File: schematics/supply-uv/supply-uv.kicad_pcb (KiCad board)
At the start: 2 copper layers, 100 x 100 mm, 88 parts, among them J1 Conn_01x02_Pin, J2 Conn_01x01_Pin, J3 CW2B-10A-T, K1 SRD-12VDC-SL-C, Q1 IRLML5203, U1 ICE2PCS01, U2 TL331, U3 R7731, U4 EL817, U5 TL432DBZ, Y1 B32022A3223M000

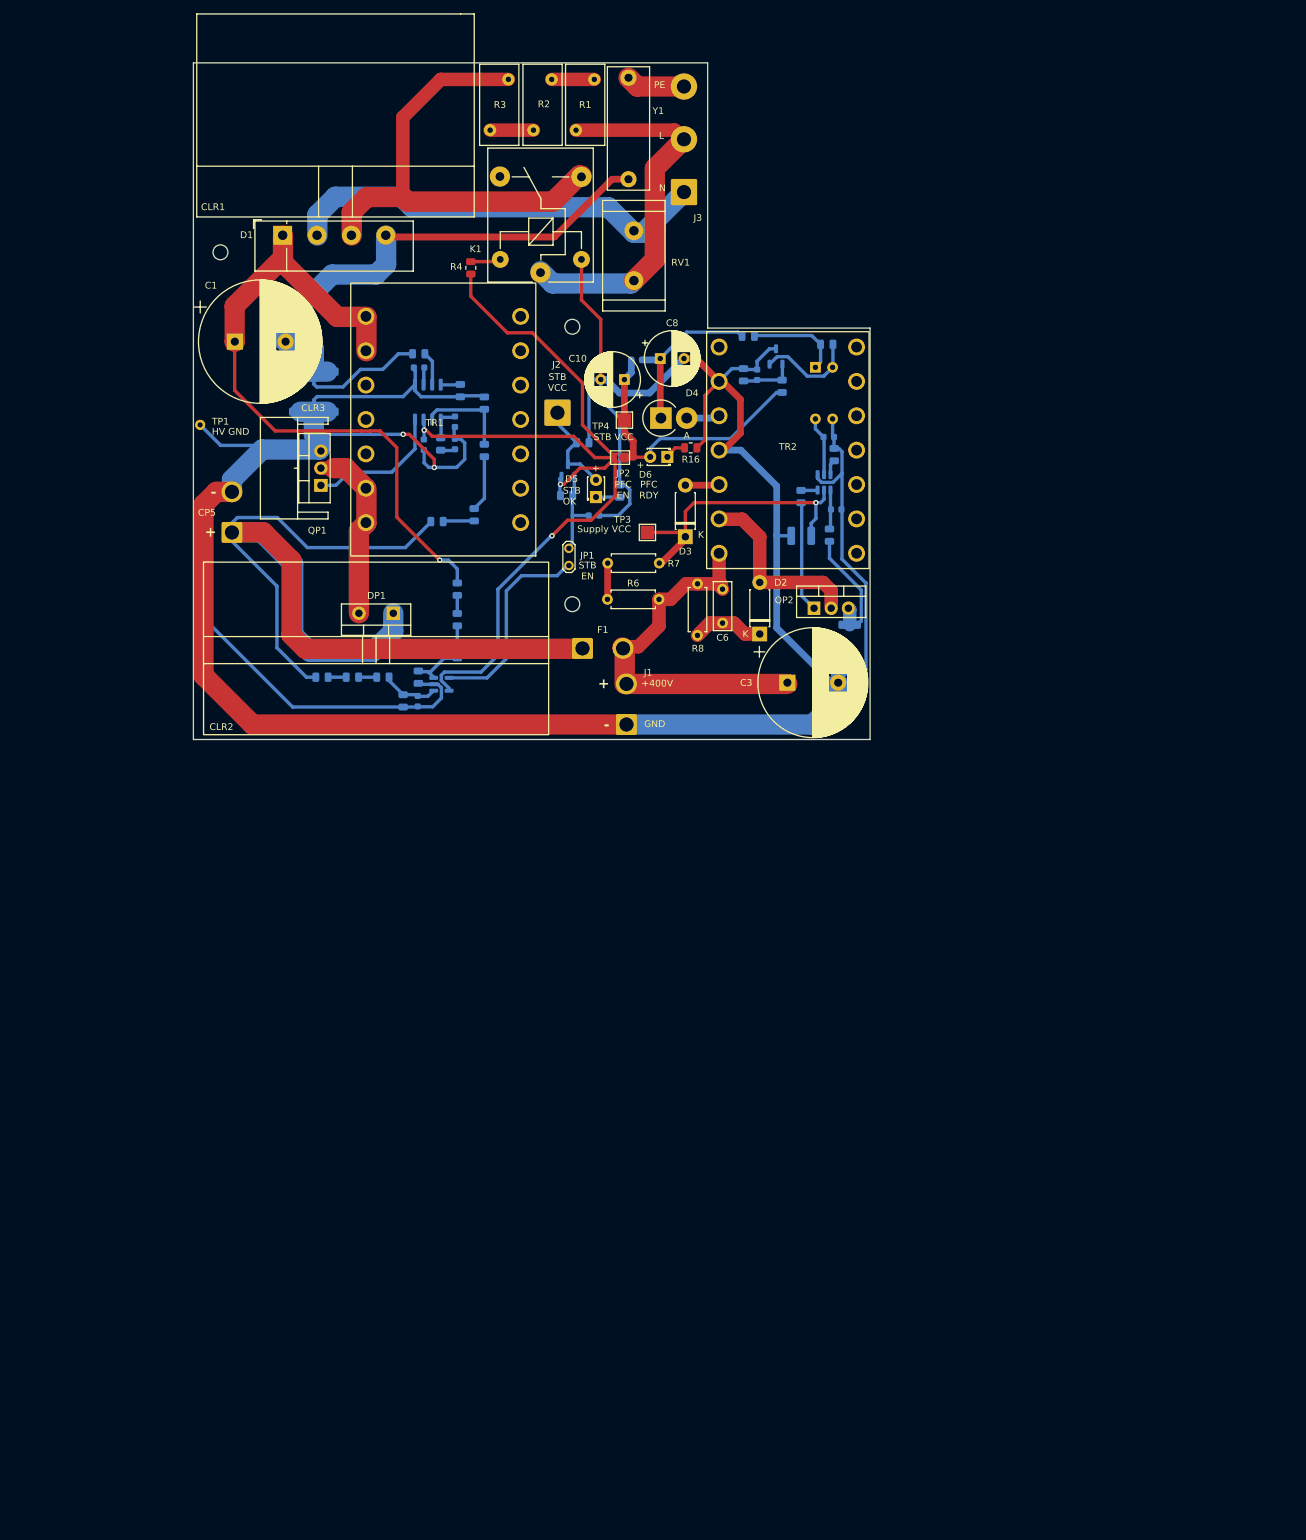
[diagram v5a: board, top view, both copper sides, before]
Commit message: Board#1 schematics rewrited
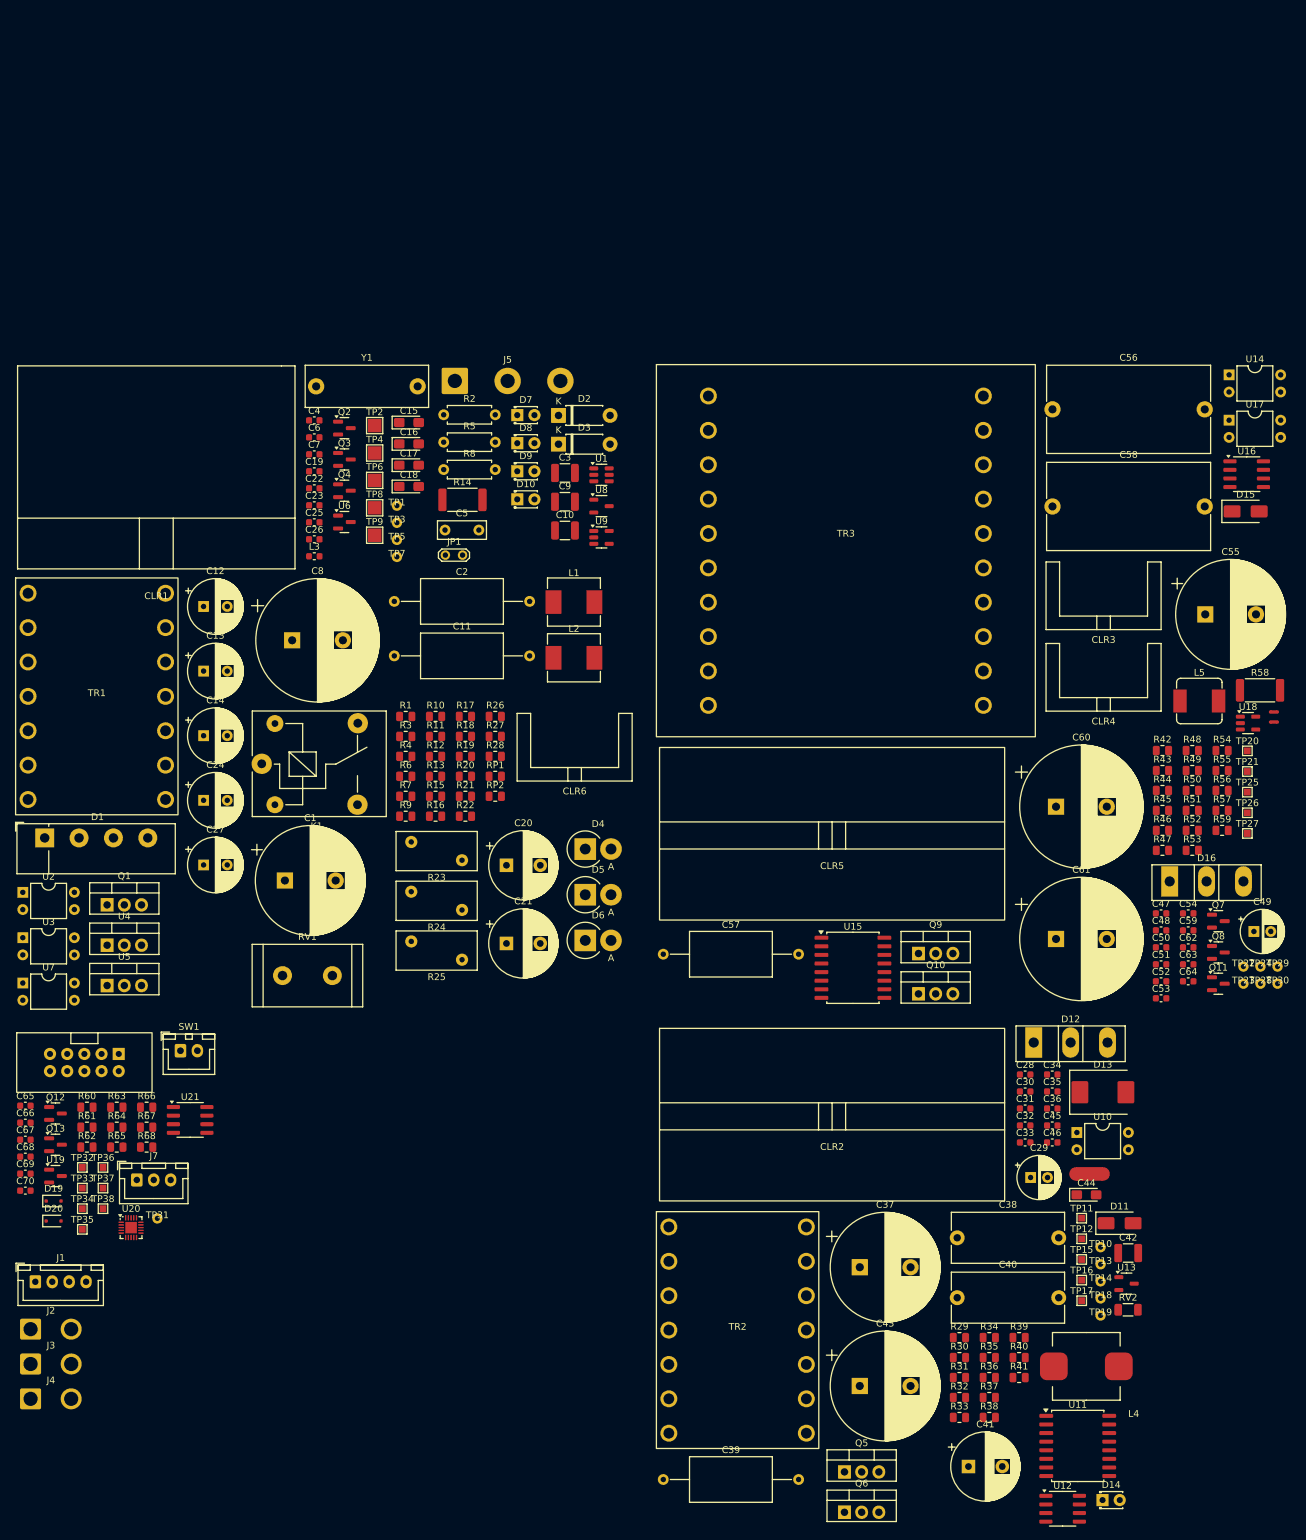
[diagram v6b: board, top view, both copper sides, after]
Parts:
- removed CP1, CP3: 100 nF, Capacitor_SMD:C_0603_1608Metric
- removed CP2, CP4: 1 uF, Capacitor_SMD:C_0603_1608Metric
- removed CP5: 3300 uF@450V, Connector_Wire:SolderWire-1.5sqmm_1x02_P6mm_D1.7mm_OD3mm
- removed DP1: STTH8S06D, Package_TO_SOT_THT:TO-220-2_Vertical
- removed F1: C10G4 with fuseholder, Connector_Wire:SolderWire-1.5sqmm_1x02_P6mm_D1.7mm_OD3mm
- removed H1, H2, H3: MountingHole, MountingHole:MountingHole_2.2mm_M2
- removed JP2: PFC Enable, Jumper:SolderJumper-2_P1.3mm_Open_TrianglePad1.0x1.5mm
- removed QP1, QP2: STP13NK60Z, Package_TO_SOT_THT:TO-220-3_Vertical
- removed RP10, RP9: 680K, Resistor_SMD:R_0805_2012Metric
- removed RP11: 620K, Resistor_SMD:R_0805_2012Metric
- removed RP12: 15K, Resistor_SMD:R_0805_2012Metric
- removed RP13, RP14, RP15, RP5, RP6, RP7: 750K, Resistor_SMD:R_0805_2012Metric
- removed RP16: 68K, Resistor_SMD:R_0805_2012Metric
- removed RP17: 0.12, Resistor_SMD:R_2512_6332Metric
- removed RP3: 10K, Resistor_SMD:R_0805_2012Metric
- removed RP4: 220, Resistor_SMD:R_0805_2012Metric
- removed RP8: 75K, Resistor_SMD:R_0805_2012Metric
- added C12: 220 uF@35V, Capacitor_THT:CP_Radial_D8.0mm_P3.50mm, F.Cu at (64.5, 124.3)
- added C13: 220 uF@35V, Capacitor_THT:CP_Radial_D8.0mm_P3.50mm, F.Cu at (64.5, 133.9)
- added C14: 220 uF@35V, Capacitor_THT:CP_Radial_D8.0mm_P3.50mm, F.Cu at (64.5, 143.4)
- added C15: 22 uF, Capacitor_Tantalum_SMD:CP_EIA-3216-10_Kemet-I_Pad1.58x1.35mm_HandSolder, F.Cu at (94.9, 97.2)
- added C16: 22 uF, Capacitor_Tantalum_SMD:CP_EIA-3216-10_Kemet-I_Pad1.58x1.35mm_HandSolder, F.Cu at (94.9, 100.3)
- added C17: 22 uF, Capacitor_Tantalum_SMD:CP_EIA-3216-10_Kemet-I_Pad1.58x1.35mm_HandSolder, F.Cu at (94.9, 103.5)
- added C18: 22 uF, Capacitor_Tantalum_SMD:CP_EIA-3216-10_Kemet-I_Pad1.58x1.35mm_HandSolder, F.Cu at (94.9, 106.6)
- added C19: 10 nF, Capacitor_SMD:C_0603_1608Metric, F.Cu at (80.9, 104.4)
- added C20: 1000 uF@16V, Capacitor_THT:CP_Radial_D10.0mm_P5.00mm, F.Cu at (109.3, 162.6)
- added C21: 1000 uF@16V, Capacitor_THT:CP_Radial_D10.0mm_P5.00mm, F.Cu at (109.3, 174.1)
- added C22: 4.7 uF, Capacitor_SMD:C_0603_1608Metric, F.Cu at (80.9, 106.9)
- added C23: 10 nF, Capacitor_SMD:C_0603_1608Metric, F.Cu at (80.9, 109.4)
- added C24: 220 uF@35V, Capacitor_THT:CP_Radial_D8.0mm_P3.50mm, F.Cu at (64.5, 153.0)
- added C25: 100 nF, Capacitor_SMD:C_0603_1608Metric, F.Cu at (80.9, 111.9)
- added C26: 1 uF, Capacitor_SMD:C_0603_1608Metric, F.Cu at (80.9, 114.4)
- added C27: 220 uF@35V, Capacitor_THT:CP_Radial_D8.0mm_P3.50mm, F.Cu at (64.5, 162.5)
- added C28: 100 nF, Capacitor_SMD:C_0603_1608Metric, F.Cu at (185.9, 193.5)
- added C29: 47 uF@35V, Capacitor_THT:CP_Radial_D6.3mm_P2.50mm, F.Cu at (186.7, 208.7)
- added C30: 10 uF, Capacitor_SMD:C_0603_1608Metric, F.Cu at (185.9, 196.0)
- added C31: 100 nF, Capacitor_SMD:C_0603_1608Metric, F.Cu at (185.9, 198.5)
- added C32: 2.2 nF, Capacitor_SMD:C_0603_1608Metric, F.Cu at (185.9, 201.0)
- added C33: 10 uF, Capacitor_SMD:C_0603_1608Metric, F.Cu at (185.9, 203.6)
- added C34: 100 nF, Capacitor_SMD:C_0603_1608Metric, F.Cu at (189.9, 193.5)
- added C35: 100 nF, Capacitor_SMD:C_0603_1608Metric, F.Cu at (189.9, 196.0)
- added C36: 1 uF, Capacitor_SMD:C_0603_1608Metric, F.Cu at (189.9, 198.5)
- added C37: 47 uF@450V, Capacitor_THT:CP_Radial_D16.0mm_P7.50mm, F.Cu at (161.5, 222.0)
- added C38: К73-17 0.15 uF@400V, Capacitor_THT:C_Rect_L16.5mm_W7.3mm_P15.00mm_MKT, F.Cu at (175.9, 217.6)
- added C39: К73-17 0.22 uF@630V, Capacitor_THT:C_Axial_L12.0mm_D6.5mm_P20.00mm_Horizontal, F.Cu at (132.4, 253.4)
- added C40: К73-17 0.15 uF@400V, Capacitor_THT:C_Rect_L16.5mm_W7.3mm_P15.00mm_MKT, F.Cu at (175.9, 226.5)
- added C41: 1000 uF@16V, Capacitor_THT:CP_Radial_D10.0mm_P5.00mm, F.Cu at (177.5, 251.4)
- added C42: 22 uF, Capacitor_SMD:C_1210_3225Metric, F.Cu at (201.2, 219.9)
- added C43: 2200 uF@35V, Capacitor_THT:CP_Radial_D16.0mm_P7.50mm, F.Cu at (161.5, 239.5)
- added C44: 22 uF, Capacitor_Tantalum_SMD:CP_EIA-3216-10_Kemet-I_Pad1.58x1.35mm_HandSolder, F.Cu at (195.0, 211.3)
- added C45: 100 nF, Capacitor_SMD:C_0603_1608Metric, F.Cu at (189.9, 201.0)
- added C46: 1 uF, Capacitor_SMD:C_0603_1608Metric, F.Cu at (189.9, 203.6)
- added C47: 100 nF, Capacitor_SMD:C_0603_1608Metric, F.Cu at (206.0, 169.7)
- added C48: 10 uF, Capacitor_SMD:C_0603_1608Metric, F.Cu at (206.0, 172.2)
- added C49: 47 uF@35V, Capacitor_THT:CP_Radial_D6.3mm_P2.50mm, F.Cu at (219.7, 172.4)
- added C50: 10 uF, Capacitor_SMD:C_0603_1608Metric, F.Cu at (206.0, 174.7)
- added C51: 2.2 nF, Capacitor_SMD:C_0603_1608Metric, F.Cu at (206.0, 177.2)
- added C52: 100 nF, Capacitor_SMD:C_0603_1608Metric, F.Cu at (206.0, 179.7)
- added C53: 100 nF, Capacitor_SMD:C_0603_1608Metric, F.Cu at (206.0, 182.2)
- added C54: 1 uF, Capacitor_SMD:C_0603_1608Metric, F.Cu at (210.0, 169.7)
- added C55: 47 uF@450V, Capacitor_THT:CP_Radial_D16.0mm_P7.50mm, F.Cu at (212.5, 125.5)
- added C56: К73-17 1 uF@400V, Capacitor_THT:C_Rect_L24.0mm_W12.8mm_P22.50mm_MKT, F.Cu at (190.0, 95.2)
- added C57: К73-17 0.22 uF@630V, Capacitor_THT:C_Axial_L12.0mm_D6.5mm_P20.00mm_Horizontal, F.Cu at (132.4, 175.7)
- added C58: К73-17 1 uF@400V, Capacitor_THT:C_Rect_L24.0mm_W12.8mm_P22.50mm_MKT, F.Cu at (190.0, 109.6)
- added C59: 100 nF, Capacitor_SMD:C_0603_1608Metric, F.Cu at (210.0, 172.2)
- added C60: 2200 uF@63V, Capacitor_THT:CP_Radial_D18.0mm_P7.50mm, F.Cu at (190.5, 153.9)
- added C61: 2200 uF@63V, Capacitor_THT:CP_Radial_D18.0mm_P7.50mm, F.Cu at (190.5, 173.5)
- added C62: 10 nF, Capacitor_SMD:C_0603_1608Metric, F.Cu at (210.0, 174.7)
- added C63: 10 nF, Capacitor_SMD:C_0603_1608Metric, F.Cu at (210.0, 177.2)
- added C64: 1 uF, Capacitor_SMD:C_0603_1608Metric, F.Cu at (210.0, 179.7)
- added C65: 100 nF, Capacitor_SMD:C_0603_1608Metric, F.Cu at (38.2, 198.1)
- added C66: 4.7 uF, Capacitor_SMD:C_0603_1608Metric, F.Cu at (38.2, 200.6)
- added C67: 220 nF, Capacitor_SMD:C_0603_1608Metric, F.Cu at (38.2, 203.1)
- added C68: 100 nF, Capacitor_SMD:C_0603_1608Metric, F.Cu at (38.2, 205.7)
- added C69: 100 nF, Capacitor_SMD:C_0603_1608Metric, F.Cu at (38.2, 208.2)
- added C70: 1 uF, Capacitor_SMD:C_0603_1608Metric, F.Cu at (38.2, 210.7)
- added CLR4: HS 239-20, Library:HS-239-20, F.Cu at (197.5, 139.8)
- added CLR5: HS 216-30@30х51х25.5mm, Library:HS 216-30, F.Cu at (157.4, 158.2)
- added CLR6: HS 239-20, Library:HS-239-20, F.Cu at (119.3, 150.1)
- added D10: L-2060YD, LED_THT:LED_D1.8mm_W3.3mm_H2.4mm, F.Cu at (110.9, 108.5)
- added D11: STTH1R06A, Diode_SMD:D_SMA, F.Cu at (199.9, 215.5)
- added D12: STTH3003CW, Package_TO_SOT_THT:TO-247-3_Vertical, F.Cu at (187.2, 188.8)
- added D13: SMCJ5.0A, Diode_SMD:D_SMC, F.Cu at (197.4, 196.1)
- added D14: L-2060YD, LED_THT:LED_D1.8mm_W3.3mm_H2.4mm, F.Cu at (197.4, 256.4)
- added D15: STTH1R06A, Diode_SMD:D_SMA, F.Cu at (218.5, 110.3)
- added D16: STTH3003CW, Package_TO_SOT_THT:TO-247-3_Vertical, F.Cu at (207.3, 165.0)
- added D19: BAV21WS, Diode_SMD:D_SOD-323F, F.Cu at (42.3, 212.2)
- added D20: BAV21WS, Diode_SMD:D_SOD-323F, F.Cu at (42.3, 215.2)
- added D7: L-2060YD, LED_THT:LED_D1.8mm_W3.3mm_H2.4mm, F.Cu at (110.9, 96.1)
- added D8: L-2060YD, LED_THT:LED_D1.8mm_W3.3mm_H2.4mm, F.Cu at (110.9, 100.2)
- added D9: L-2060YD, LED_THT:LED_D1.8mm_W3.3mm_H2.4mm, F.Cu at (110.9, 104.4)
- added J4: PWR_OUT (with fuse), Connector_Wire:SolderWire-1.5sqmm_1x02_P6mm_D1.7mm_OD3mm, F.Cu at (38.9, 241.4)
- added J5: CW2B-10A-T, Connector_Wire:SolderWire-1.5sqmm_1x03_P7.8mm_D1.7mm_OD3.9mm, F.Cu at (101.6, 91.0)
- added J6: USBASP, Library:DC3-2x05_p2.54, F.Cu at (46.9, 191.7)
- added J7: JST XH B3B, Connector_JST:JST_XH_B3B-XH-A_1x03_P2.50mm_Vertical, F.Cu at (54.6, 209.1)
- added L2: 22 uH@0650, Inductor_SMD:L_Chilisin_BMRB00060650, F.Cu at (119.2, 131.9)
- added L3: BLM18EG221SN1D, Inductor_SMD:L_0603_1608Metric, F.Cu at (80.9, 116.9)
- added L4: HPI1040-1R0, Library:Ferrocore-HPI1040, F.Cu at (195.0, 236.6)
- added L5: SPM6550T-R68M, Inductor_SMD:L_Sumida_CDMC6D28_7.25x6.5mm, F.Cu at (211.7, 138.3)
- added NT1: STB2HV_GND, NetTie:NetTie-2_SMD_Pad2.0mm, F.Cu at (195.4, 208.2)
- added NT2: STB2HV_GND, NetTie:NetTie-2_SMD_Pad0.5mm, F.Cu at (222.7, 139.9)
- added NT3: VSYS_PWR2PWR_OUT_GND, NetTie:NetTie-2_SMD_Pad0.5mm, F.Cu at (222.7, 141.4)
- added Q10: STP13NK60Z, Package_TO_SOT_THT:TO-220-3_Vertical, F.Cu at (170.2, 181.6)
- added Q11: IRLML0030, Package_TO_SOT_SMD:SOT-23, F.Cu at (214.5, 180.1)
- added Q12: IRLML0030, Package_TO_SOT_SMD:SOT-23, F.Cu at (42.6, 199.3)
- added Q13: IRLML0030, Package_TO_SOT_SMD:SOT-23, F.Cu at (42.6, 203.9)
- added Q2: IRLML5203, Package_TO_SOT_SMD:SOT-23, F.Cu at (85.3, 98.0)
- added Q3: IRLML5203, Package_TO_SOT_SMD:SOT-23, F.Cu at (85.3, 102.6)
- added Q4: IRLML5203, Package_TO_SOT_SMD:SOT-23, F.Cu at (85.3, 107.2)
- added Q5: STP13NK60Z, Package_TO_SOT_THT:TO-220-3_Vertical, F.Cu at (159.2, 252.2)
- added Q6: STP13NK60Z, Package_TO_SOT_THT:TO-220-3_Vertical, F.Cu at (159.2, 258.2)
- added Q7: IRLML0030, Package_TO_SOT_SMD:SOT-23, F.Cu at (214.5, 170.8)
- added Q8: IRLML0030, Package_TO_SOT_SMD:SOT-23, F.Cu at (214.5, 175.5)
- added Q9: STP13NK60Z, Package_TO_SOT_THT:TO-220-3_Vertical, F.Cu at (170.2, 175.6)
- added R20: 39K, Resistor_SMD:R_0805_2012Metric, F.Cu at (103.2, 149.4)
- added R21: 3K, Resistor_SMD:R_0805_2012Metric, F.Cu at (103.2, 152.4)
- added R22: 1K, Resistor_SMD:R_0805_2012Metric, F.Cu at (103.2, 155.3)
- added R23: JNR13S500L, Varistor:RV_Disc_D12mm_W5.8mm_P7.5mm, F.Cu at (95.2, 159.1)
- added R24: JNR13S500L, Varistor:RV_Disc_D12mm_W5.8mm_P7.5mm, F.Cu at (95.2, 166.5)
- added R25: JNR13S500L, Varistor:RV_Disc_D12mm_W5.8mm_P7.5mm, F.Cu at (95.2, 173.8)
- added R26: 150, Resistor_SMD:R_0805_2012Metric, F.Cu at (107.6, 140.6)
- added R27: 10K, Resistor_SMD:R_0805_2012Metric, F.Cu at (107.6, 143.5)
- added R28: 1K, Resistor_SMD:R_0805_2012Metric, F.Cu at (107.6, 146.5)
- added R29: 680, Resistor_SMD:R_0805_2012Metric, F.Cu at (176.2, 232.4)
- added R30: 2K, Resistor_SMD:R_0805_2012Metric, F.Cu at (176.2, 235.3)
- added R31: 10K, Resistor_SMD:R_0805_2012Metric, F.Cu at (176.2, 238.3)
- added R32: 10K, Resistor_SMD:R_0805_2012Metric, F.Cu at (176.2, 241.2)
- added R33: 4K7, Resistor_SMD:R_0805_2012Metric, F.Cu at (176.2, 244.2)
- added R34: 2K2, Resistor_SMD:R_0805_2012Metric, F.Cu at (180.6, 232.4)
- added R35: 22, Resistor_SMD:R_0805_2012Metric, F.Cu at (180.6, 235.3)
- added R36: 10, Resistor_SMD:R_0805_2012Metric, F.Cu at (180.6, 238.3)
- added R37: 10, Resistor_SMD:R_0805_2012Metric, F.Cu at (180.6, 241.2)
- added R38: 150, Resistor_SMD:R_0805_2012Metric, F.Cu at (180.6, 244.2)
- added R39: 10K, Resistor_SMD:R_0805_2012Metric, F.Cu at (185.0, 232.4)
- added R40: 3K3, Resistor_SMD:R_0805_2012Metric, F.Cu at (185.0, 235.3)
- added R41: 510, Resistor_SMD:R_0805_2012Metric, F.Cu at (185.0, 238.3)
- added R42: 10K, Resistor_SMD:R_0805_2012Metric, F.Cu at (206.2, 145.6)
- added R43: 10K, Resistor_SMD:R_0805_2012Metric, F.Cu at (206.2, 148.6)
- added R44: 2K, Resistor_SMD:R_0805_2012Metric, F.Cu at (206.2, 151.5)
- added R45: 2K2, Resistor_SMD:R_0805_2012Metric, F.Cu at (206.2, 154.5)
- added R46: 10K, Resistor_SMD:R_0805_2012Metric, F.Cu at (206.2, 157.4)
- added R47: 22, Resistor_SMD:R_0805_2012Metric, F.Cu at (206.2, 160.4)
- added R48: 2K, Resistor_SMD:R_0805_2012Metric, F.Cu at (210.6, 145.6)
- added R49: 10K, Resistor_SMD:R_0805_2012Metric, F.Cu at (210.6, 148.6)
- added R50: 10K, Resistor_SMD:R_0805_2012Metric, F.Cu at (210.6, 151.5)
- added R51: 10, Resistor_SMD:R_0805_2012Metric, F.Cu at (210.6, 154.5)
- added R52: 10, Resistor_SMD:R_0805_2012Metric, F.Cu at (210.6, 157.4)
- added R53: 2K, Resistor_SMD:R_0805_2012Metric, F.Cu at (210.6, 160.4)
- added R54: 2K, Resistor_SMD:R_0805_2012Metric, F.Cu at (215.0, 145.6)
- added R55: 10K, Resistor_SMD:R_0805_2012Metric, F.Cu at (215.0, 148.6)
- added R56: 9K1, Resistor_SMD:R_0805_2012Metric, F.Cu at (215.0, 151.5)
- added R57: 1K, Resistor_SMD:R_0805_2012Metric, F.Cu at (215.0, 154.5)
- added R58: 0.01, Resistor_SMD:R_2512_6332Metric, F.Cu at (220.6, 136.7)
- added R59: 47K, Resistor_SMD:R_0805_2012Metric, F.Cu at (215.0, 157.4)
- added R60: 510, Resistor_SMD:R_0805_2012Metric, F.Cu at (47.3, 198.3)
- added R61: 10K, Resistor_SMD:R_0805_2012Metric, F.Cu at (47.3, 201.3)
- added R62: 10K, Resistor_SMD:R_0805_2012Metric, F.Cu at (47.3, 204.2)
- added R63: 220, Resistor_SMD:R_0805_2012Metric, F.Cu at (51.7, 198.3)
- added R64: 10K, Resistor_SMD:R_0805_2012Metric, F.Cu at (51.7, 201.3)
- added R65: 220, Resistor_SMD:R_0805_2012Metric, F.Cu at (51.7, 204.2)
- added R66: 10K, Resistor_SMD:R_0805_2012Metric, F.Cu at (56.1, 198.3)
- added R67: 10K, Resistor_SMD:R_0805_2012Metric, F.Cu at (56.1, 201.3)
- added R68: 10K, Resistor_SMD:R_0805_2012Metric, F.Cu at (56.1, 204.2)
- added RV2: CT1206M6G, Resistor_SMD:R_1206_3216Metric, F.Cu at (201.1, 228.3)
- added SW1: SW_Push, Connector_JST:JST_XH_B2B-XH-A_1x02_P2.50mm_Vertical, F.Cu at (61.1, 190.0)
- added TP10: +5V_FEEDBACK, Library:TestPoint_Plated_Hole_D1.0mm, F.Cu at (197.1, 219.0)
- added TP11: 5V_H, TestPoint:TestPoint_Pad_1.0x1.0mm, F.Cu at (194.3, 214.7)
- added TP12: 5V_L, TestPoint:TestPoint_Pad_1.0x1.0mm, F.Cu at (194.3, 217.8)
- added TP13: STB_GND, Library:TestPoint_Plated_Hole_D1.0mm, F.Cu at (197.1, 221.6)
- added TP14: HV_GND, Library:TestPoint_Plated_Hole_D1.0mm, F.Cu at (197.1, 224.1)
- added TP15: 5V_GH, TestPoint:TestPoint_Pad_1.0x1.0mm, F.Cu at (194.3, 220.8)
- added TP16: 5V_GL, TestPoint:TestPoint_Pad_1.0x1.0mm, F.Cu at (194.3, 223.9)
- added TP17: 5V_MP, TestPoint:TestPoint_Pad_1.0x1.0mm, F.Cu at (194.3, 226.9)
- added TP18: +5V_PWR, Library:TestPoint_Plated_Hole_D1.0mm, F.Cu at (197.1, 226.6)
- added TP19: +5V_GND, Library:TestPoint_Plated_Hole_D1.0mm, F.Cu at (197.1, 229.1)
- added TP2: Supply VCC, TestPoint:TestPoint_Pad_2.0x2.0mm, F.Cu at (89.8, 97.6)
- added TP20: PV_H, TestPoint:TestPoint_Pad_1.0x1.0mm, F.Cu at (218.8, 145.7)
- added TP21: PV_L, TestPoint:TestPoint_Pad_1.0x1.0mm, F.Cu at (218.8, 148.7)
- added TP22: PWR_SHUTDOWN, Library:TestPoint_Plated_Hole_D1.0mm, F.Cu at (218.2, 177.6)
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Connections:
- net Net-(D5-K) renamed /standby Sheet/VSYS1_PRE_VCC
- C1 pad 1: /Input power with filter/VOUT_PRE_PFC -> /5V_PWR Sheet/HV_VCC
- C1 pad 2: /Input power with filter/VOUT_PRE_GND -> /5V_PWR Sheet/HV_GND
- C10 pad 1: Net-(D6-A) -> /pwrcontrol Sheet/VSYS_PWR_GND
- C10 pad 2: /Input power with filter/HV_GND -> Net-(Q3-D)
- C11 pad 1: /Input power with filter/HV_GND -> /5V_PWR Sheet/HV_GND
- C11 pad 2: Net-(JP1-B) -> /5V_PWR Sheet/HV_VCC
- C2 pad 1: Net-(U2--) -> /5V_PWR Sheet/HV_GND
- C2 pad 2: /Input power with filter/HV_GND -> /5V_PWR Sheet/HV_VCC
- C3 pad 1: /Input power with filter/OUT_400V -> /5V_PWR Sheet/HV_GND
- C3 pad 2: /Input power with filter/HV_GND -> Net-(D2-K)
- C4 pad 1: /Input power with filter/HV_GND -> /5V_PWR Sheet/HV_GND
- C4 pad 2: Net-(D3-K) -> Net-(U1-CS)
- C5 pad 1: /Input power with filter/HV_GND -> Net-(D3-K)
- C5 pad 2: Net-(U3-CS) -> /5V_PWR Sheet/HV_VCC
- C6 pad 1: Net-(D2-K) -> /VSYS_GND
- C6 pad 2: /Input power with filter/OUT_400V -> Net-(Q2-G)
- C7 pad 1: /Input power with filter/HV_GND -> /pwrcontrol Sheet/VSYS_PWR_GND
- C7 pad 2: /Standby Supply/FEEDBACK -> Net-(Q3-G)
- C8 pad 1: Net-(D4-K) -> /5V_PWR Sheet/HV_VCC
- C8 pad 2: /Input power with filter/HV_GND -> /5V_PWR Sheet/HV_GND
- C9 pad 1: /Input power with filter/HV_GND -> /VSYS_GND
- C9 pad 2: Net-(U5-REF) -> Net-(Q2-D)
- D1 pad 1: /Input power with filter/VOUT_PRE_PFC -> /5V_PWR Sheet/HV_VCC
- D1 pad 2: Net-(J3-Pin_1) -> Net-(J5-Pin_1)
- D1 pad 3: /Input power with filter/STARTUP_PROTECT_OUT -> /standby Sheet/STARTUP_PROTECT_OUT
- D1 pad 4: /Input power with filter/VOUT_PRE_GND -> /5V_PWR Sheet/HV_GND
- D5 pad 2: /Standby Supply/V_STANDBY -> Net-(D5-A)
- D6 pad 1: Net-(D6-K) -> /standby Sheet/VSYS2_PRE_VCC
- J1 pad 1: /Input power with filter/HV_GND -> /VSYS_SCL
- J1 pad 2: /Input power with filter/OUT_400V -> /VSYS_SDA
- J2 pad 1: /Standby Supply/V_STANDBY -> /+5V_PWR_VCC
- J3 pad 1: Net-(J3-Pin_1) -> /+5V_PWR_VCC
- J3 pad 2: /Input power with filter/STARTUP_PROTECT_IN -> /+5V_PWR_GND
- JP1 pad 1: /Input power with filter/PFC_OK# -> Net-(D9-A)
- JP1 pad 2: Net-(JP1-B) -> /standby Sheet/V_STANDBY_PRE
- K1 pad 1: /Input power with filter/STARTUP_PROTECT_IN -> /standby Sheet/STARTUP_PROTECT_IN
- K1 pad 2: /Input power with filter/HV_GND -> /5V_PWR Sheet/HV_GND
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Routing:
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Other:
- board outline removed
- board text removed: "+"
- board text removed: "+400V"
- board text removed: "-"
- board text removed: "GND"
- board text removed: "L"
- board text removed: "N"
- board text removed: "PE"
- board text removed: "PFC EN"
- board text removed: "PFC RDY"
- board text removed: "STB EN"
- board text removed: "STB OK"
- board text removed: "STB VCC"
- board text removed: "Supply board#1 v1.3"

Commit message: start board#1 tracing
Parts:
- added C71: 4.7 uF, Capacitor_SMD:C_0603_1608Metric, F.Cu at (-31.2, 111.9)
- added C72: 220 nF, Capacitor_SMD:C_0603_1608Metric, B.Cu at (-26.4, 113.7)
- added C73: 1 uF, Capacitor_SMD:C_0603_1608Metric, F.Cu at (-33.3, 127.2)
- added D17: SMCJ5.0A, Diode_SMD:D_SMC, F.Cu at (-73.1, 266.1)
- added D18: L-2060YD, LED_THT:LED_D1.8mm_W3.3mm_H2.4mm, F.Cu at (-59.0, 202.9)
- added D21: STTH3003CW, Package_TO_SOT_THT:TO-247-3_Vertical, F.Cu at (92.2, 189.7)
- added D24: BAV21WS, Diode_SMD:D_SOD-323F, B.Cu at (-38.5, 116.5)
- added D25: BAV21WS, Diode_SMD:D_SOD-323F, B.Cu at (-36.3, 116.5)
- added F3: 1.5A, Library:FuseHolder1808, F.Cu at (-97.0, 44.6)
- added F4: 1A, Library:FuseHolder1808, F.Cu at (-178.6, 56.2)
- added F5: 5A, Library:FuseHolder1808, F.Cu at (181.4, 249.7)
- added H1: MountingHole, MountingHole:MountingHole_2.2mm_M2, F.Cu at (633.3, 236.1)
- added JP2: VSYS2_EN, Jumper:SolderJumper-2_P1.3mm_Open_TrianglePad1.0x1.5mm, F.Cu at (-17.8, 87.2)
- added JP3: STB_EN, TestPoint:TestPoint_2Pads_Pitch2.54mm_Drill0.8mm, F.Cu at (-46.0, 38.0)
- added JP4: 5V_EN, Jumper:SolderJumper-2_P1.3mm_Open_TrianglePad1.0x1.5mm, F.Cu at (-48.6, 49.4)
- added JP5: PWR_EN, Jumper:SolderJumper-2_P1.3mm_Open_TrianglePad1.0x1.5mm, F.Cu at (-48.6, 52.8)
- added Q14: IRLML0030, Package_TO_SOT_SMD:SOT-23, F.Cu at (-29.4, 123.4)
- added R69: 220, Resistor_SMD:R_0805_2012Metric, F.Cu at (-24.5, 126.3)
- added R70: 10K, Resistor_SMD:R_0805_2012Metric, F.Cu at (-29.4, 120.1)
- added R71: 220, Resistor_SMD:R_0805_2012Metric, F.Cu at (-24.6, 128.5)
- added R72: 10K, Resistor_SMD:R_0805_2012Metric, F.Cu at (-36.4, 116.5)
- added R73: 10K, Resistor_SMD:R_0805_2012Metric, F.Cu at (-38.5, 116.5)
- added R74: 10K, Resistor_SMD:R_0805_2012Metric, B.Cu at (-35.4, 119.8)
- added U22: ATtiny1616-M, Package_DFN_QFN:VQFN-20-1EP_3x3mm_P0.4mm_EP1.7x1.7mm, B.Cu at (-32.9, 112.6)
- C1: value 47 uF@450V -> 100 nF; footprint Capacitor_THT:CP_Radial_D16.0mm_P7.50mm -> Capacitor_SMD:C_0603_1608Metric; moved to B.Cu
- C10: value 22 uF -> 100 uF@350V; footprint Capacitor_SMD:C_1210_3225Metric -> Capacitor_THT:CP_Radial_D18.0mm_P7.50mm
- C11: value К73-17 0.22 uF@630V -> 22 uF; footprint Capacitor_THT:C_Axial_L12.0mm_D6.5mm_P20.00mm_Horizontal -> Capacitor_SMD:C_1210_3225Metric; moved to B.Cu
- C12: value 220 uF@35V -> 22 uF; footprint Capacitor_THT:CP_Radial_D8.0mm_P3.50mm -> Capacitor_SMD:C_1210_3225Metric
- C13: value 220 uF@35V -> К73-17 0.22 uF@630V; footprint Capacitor_THT:CP_Radial_D8.0mm_P3.50mm -> Capacitor_THT:C_Axial_L12.0mm_D6.5mm_P20.00mm_Horizontal
- C15, C16: value 22 uF -> 220 uF@35V; footprint Capacitor_Tantalum_SMD:CP_EIA-3216-10_Kemet-I_Pad1.58x1.35mm_HandSolder -> Capacitor_THT:CP_Radial_D8.0mm_P3.50mm
- C17, L3, Q2, Q3, Q4, R1, R10, R11, R12, R13, R14, R20, R21, R26, R27, R28, R67, R9, RP1, RP2: moved to B.Cu
- C19: value 10 nF -> 22 uF; footprint Capacitor_SMD:C_0603_1608Metric -> Capacitor_Tantalum_SMD:CP_EIA-3216-10_Kemet-I_Pad1.58x1.35mm_HandSolder; moved to B.Cu
- C2: value К73-17 0.22 uF@630V -> 100 nF; footprint Capacitor_THT:C_Axial_L12.0mm_D6.5mm_P20.00mm_Horizontal -> Capacitor_SMD:C_0603_1608Metric; moved to B.Cu
- C20: value 1000 uF@16V -> 22 uF; footprint Capacitor_THT:CP_Radial_D10.0mm_P5.00mm -> Capacitor_Tantalum_SMD:CP_EIA-3216-10_Kemet-I_Pad1.58x1.35mm_HandSolder; moved to B.Cu
- C21: value 1000 uF@16V -> 10 nF; footprint Capacitor_THT:CP_Radial_D10.0mm_P5.00mm -> Capacitor_SMD:C_0603_1608Metric; moved to B.Cu
- C22: value 4.7 uF -> 1000 uF@16V; footprint Capacitor_SMD:C_0603_1608Metric -> Capacitor_THT:CP_Radial_D10.0mm_P5.00mm
- C23: value 10 nF -> 1000 uF@16V; footprint Capacitor_SMD:C_0603_1608Metric -> Capacitor_THT:CP_Radial_D10.0mm_P5.00mm
- C24: value 220 uF@35V -> 4.7 uF; footprint Capacitor_THT:CP_Radial_D8.0mm_P3.50mm -> Capacitor_SMD:C_0603_1608Metric
- C25, C6: value 100 nF -> 10 nF; moved to B.Cu
- C26: value 1 uF -> 220 uF@35V; footprint Capacitor_SMD:C_0603_1608Metric -> Capacitor_THT:CP_Radial_D8.0mm_P3.50mm
- C27: value 220 uF@35V -> 100 nF; footprint Capacitor_THT:CP_Radial_D8.0mm_P3.50mm -> Capacitor_SMD:C_0603_1608Metric; moved to B.Cu
- C28: value 100 nF -> 1 uF; moved to B.Cu
- C29: value 47 uF@35V -> 220 uF@35V; footprint Capacitor_THT:CP_Radial_D6.3mm_P2.50mm -> Capacitor_THT:CP_Radial_D8.0mm_P3.50mm
- C3: value 22 uF -> 47 uF@450V; footprint Capacitor_SMD:C_1210_3225Metric -> Capacitor_THT:CP_Radial_D16.0mm_P7.50mm
- C30, C48: value 10 uF -> 100 nF
- C32, C51: value 2.2 nF -> 47 uF@35V; footprint Capacitor_SMD:C_0603_1608Metric -> Capacitor_THT:CP_Radial_D6.3mm_P2.50mm
- C35: value 100 nF -> 2.2 nF
- C36, C54: value 1 uF -> 10 uF
- C37: value 47 uF@450V -> 100 nF; footprint Capacitor_THT:CP_Radial_D16.0mm_P7.50mm -> Capacitor_SMD:C_0603_1608Metric
- C38: value К73-17 0.15 uF@400V -> 100 nF; footprint Capacitor_THT:C_Rect_L16.5mm_W7.3mm_P15.00mm_MKT -> Capacitor_SMD:C_0603_1608Metric
- C39: value К73-17 0.22 uF@630V -> 1 uF; footprint Capacitor_THT:C_Axial_L12.0mm_D6.5mm_P20.00mm_Horizontal -> Capacitor_SMD:C_0603_1608Metric
- C4, C62: value 10 nF -> К73-17 0.22 uF@630V; footprint Capacitor_SMD:C_0603_1608Metric -> Capacitor_THT:C_Axial_L12.0mm_D6.5mm_P20.00mm_Horizontal
- C40: value К73-17 0.15 uF@400V -> 47 uF@450V; footprint Capacitor_THT:C_Rect_L16.5mm_W7.3mm_P15.00mm_MKT -> Capacitor_THT:CP_Radial_D16.0mm_P7.50mm
- C41: value 1000 uF@16V -> К73-17 0.15 uF@400V; footprint Capacitor_THT:CP_Radial_D10.0mm_P5.00mm -> Capacitor_THT:C_Rect_L16.5mm_W7.3mm_P15.00mm_MKT
- C42: value 22 uF -> К73-17 0.22 uF@630V; footprint Capacitor_SMD:C_1210_3225Metric -> Capacitor_THT:C_Axial_L12.0mm_D6.5mm_P20.00mm_Horizontal
- C43: value 2200 uF@35V -> К73-17 0.15 uF@400V; footprint Capacitor_THT:CP_Radial_D16.0mm_P7.50mm -> Capacitor_THT:C_Rect_L16.5mm_W7.3mm_P15.00mm_MKT
- C44: value 22 uF -> 1000 uF@16V; footprint Capacitor_Tantalum_SMD:CP_EIA-3216-10_Kemet-I_Pad1.58x1.35mm_HandSolder -> Capacitor_THT:CP_Radial_D10.0mm_P5.00mm
- C45: value 100 nF -> 22 uF; footprint Capacitor_SMD:C_0603_1608Metric -> Capacitor_SMD:C_1210_3225Metric
- C46: value 1 uF -> 2200 uF@35V; footprint Capacitor_SMD:C_0603_1608Metric -> Capacitor_THT:CP_Radial_D16.0mm_P7.50mm
- C47: value 100 nF -> 22 uF; footprint Capacitor_SMD:C_0603_1608Metric -> Capacitor_Tantalum_SMD:CP_EIA-3216-10_Kemet-I_Pad1.58x1.35mm_HandSolder
- C49: value 47 uF@35V -> 1 uF; footprint Capacitor_THT:CP_Radial_D6.3mm_P2.50mm -> Capacitor_SMD:C_0603_1608Metric
- C5: value JYC3D101KBY -> 22 uF; footprint Capacitor_THT:C_Disc_D7.0mm_W2.5mm_P5.00mm -> Capacitor_SMD:C_1210_3225Metric; moved to B.Cu
- C55: value 47 uF@450V -> 2.2 nF; footprint Capacitor_THT:CP_Radial_D16.0mm_P7.50mm -> Capacitor_SMD:C_0603_1608Metric
- C56: value К73-17 1 uF@400V -> 100 nF; footprint Capacitor_THT:C_Rect_L24.0mm_W12.8mm_P22.50mm_MKT -> Capacitor_SMD:C_0603_1608Metric
- C57: value К73-17 0.22 uF@630V -> 100 nF; footprint Capacitor_THT:C_Axial_L12.0mm_D6.5mm_P20.00mm_Horizontal -> Capacitor_SMD:C_0603_1608Metric
- C58: value К73-17 1 uF@400V -> 1 uF; footprint Capacitor_THT:C_Rect_L24.0mm_W12.8mm_P22.50mm_MKT -> Capacitor_SMD:C_0603_1608Metric
- C59: value 100 nF -> 47 uF@450V; footprint Capacitor_SMD:C_0603_1608Metric -> Capacitor_THT:CP_Radial_D16.0mm_P7.50mm
- C60: value 2200 uF@63V -> К73-17 1 uF@400V; footprint Capacitor_THT:CP_Radial_D18.0mm_P7.50mm -> Capacitor_THT:C_Rect_L24.0mm_W12.8mm_P22.50mm_MKT
- C61: value 2200 uF@63V -> 100 nF; footprint Capacitor_THT:CP_Radial_D18.0mm_P7.50mm -> Capacitor_SMD:C_0603_1608Metric
- C63: value 10 nF -> К73-17 1 uF@400V; footprint Capacitor_SMD:C_0603_1608Metric -> Capacitor_THT:C_Rect_L24.0mm_W12.8mm_P22.50mm_MKT
- C64: value 1 uF -> 100 nF
- C65: value 100 nF -> 2200 uF@63V; footprint Capacitor_SMD:C_0603_1608Metric -> Capacitor_THT:CP_Radial_D18.0mm_P7.50mm
- C66: value 4.7 uF -> 2200 uF@63V; footprint Capacitor_SMD:C_0603_1608Metric -> Capacitor_THT:CP_Radial_D18.0mm_P7.50mm
- C67: value 220 nF -> 10 nF
- C68: value 100 nF -> 10 nF
- C69: value 100 nF -> 1 uF
- C7: value 100 nF -> JYC3D101KBY; footprint Capacitor_SMD:C_0603_1608Metric -> Capacitor_THT:C_Disc_D7.0mm_W2.5mm_P5.00mm
- C70: value 1 uF -> 100 nF; moved to B.Cu
- C8: value 100 uF@350V -> 100 nF; footprint Capacitor_THT:CP_Radial_D18.0mm_P7.50mm -> Capacitor_SMD:C_0603_1608Metric; moved to B.Cu
- C9: value 22 uF -> 100 nF; footprint Capacitor_SMD:C_1210_3225Metric -> Capacitor_SMD:C_0603_1608Metric; moved to B.Cu
- CLR2, CLR5: value HS 216-30@30х51х25.5mm -> HS 239-20; footprint Library:HS 216-30 -> Library:HS-239-20
- CLR3, CLR6: value HS 239-20 -> HS 216-30@30х51х25.5mm; footprint Library:HS-239-20 -> Library:HS 216-30
- D11: value STTH1R06A -> L-2060YD; footprint Diode_SMD:D_SMA -> LED_THT:LED_D1.8mm_W3.3mm_H2.4mm
- D12: value STTH3003CW -> L-2060YD; footprint Package_TO_SOT_THT:TO-247-3_Vertical -> LED_THT:LED_D1.8mm_W3.3mm_H2.4mm
- D13: value SMCJ5.0A -> L-2060YD; footprint Diode_SMD:D_SMC -> LED_THT:LED_D1.8mm_W3.3mm_H2.4mm
- D14: value L-2060YD -> SMBJ3.3A; footprint LED_THT:LED_D1.8mm_W3.3mm_H2.4mm -> Diode_SMD:D_SMB
- D19: value BAV21WS -> SMBJ3.3A; footprint Diode_SMD:D_SOD-323F -> Diode_SMD:D_SMB
- D2: value FR107 -> SMBJ3.3A; footprint Diode_THT:D_DO-41_SOD81_P7.62mm_Horizontal -> Diode_SMD:D_SMB; moved to B.Cu
- D20: value BAV21WS -> STTH1R06A; footprint Diode_SMD:D_SOD-323F -> Diode_SMD:D_SMA
- D4: value FR303 -> FR107; footprint Diode_THT:D_DO-201AD_P3.81mm_Vertical_AnodeUp -> Diode_THT:D_DO-41_SOD81_P7.62mm_Horizontal
- D7: value L-2060YD -> FR303; footprint LED_THT:LED_D1.8mm_W3.3mm_H2.4mm -> Diode_THT:D_DO-201AD_P3.81mm_Vertical_AnodeUp
- D8: value L-2060YD -> SMAJ5.0CA-TR; footprint LED_THT:LED_D1.8mm_W3.3mm_H2.4mm -> Diode_SMD:D_SMA
- D9: value L-2060YD -> SMAJ5.0CA-TR; footprint LED_THT:LED_D1.8mm_W3.3mm_H2.4mm -> Diode_SMD:D_SMA; moved to B.Cu
- JP1: value STB_EN -> VSYS1_EN; footprint TestPoint:TestPoint_2Pads_Pitch2.54mm_Drill0.8mm -> Jumper:SolderJumper-2_P1.3mm_Open_TrianglePad1.0x1.5mm
- Q11: value IRLML0030 -> STP13NK60Z; footprint Package_TO_SOT_SMD:SOT-23 -> Package_TO_SOT_THT:TO-220-3_Vertical
- Q8: value IRLML0030 -> IRLML5203
- Q9: value STP13NK60Z -> IRLML0030; footprint Package_TO_SOT_THT:TO-220-3_Vertical -> Package_TO_SOT_SMD:SOT-23
- R16, R17: value 510 -> 2K; moved to B.Cu
- R18, R19: value 2K -> 510; moved to B.Cu
- R31: value 10K -> 220
- R33: value 4K7 -> 10K
- R34: value 2K2 -> 4K7
- R35: value 22 -> 2K2
- R36: value 10 -> 22
- R38: value 150 -> 10
- R39: value 10K -> 0.5R; footprint Resistor_SMD:R_0805_2012Metric -> Resistor_SMD:R_2512_6332Metric
- R40: value 3K3 -> 150
- R41: value 510 -> 10K
- R42: value 10K -> 3K3
- R43, R66: value 10K -> 510
- R44: value 2K -> 220
- R45: value 2K2 -> 2K
- R46: value 10K -> 2K2
- R47: value 22 -> 10K
- R48, R54: value 2K -> 10K
- R50: value 10K -> 22
- R51: value 10 -> 2K
- R52: value 10 -> 10K
- R53: value 2K -> 110K
- R56: value 9K1 -> 10
- R57: value 1K -> 10
- R58: value 0.01 -> 0.04R
- R59: value 47K -> 2K
- R60: value 510 -> 2K
- R62: value 10K -> 9K1
- R63: value 220 -> 1K
- R64: value 10K -> 0.01; footprint Resistor_SMD:R_0805_2012Metric -> Resistor_SMD:R_2512_6332Metric
- R65: value 220 -> 47K
- TP10, TP18: footprint Library:TestPoint_Plated_Hole_D1.0mm -> TestPoint:TestPoint_Pad_2.0x2.0mm
- U1: value R7731 -> ISO1540; footprint Package_TO_SOT_SMD:SOT-23-6 -> Package_SO:SOIC-8_3.9x4.9mm_P1.27mm; moved to B.Cu
- U10: value EL817 -> TL331; footprint Package_DIP:DIP-4_W7.62mm -> Package_TO_SOT_SMD:SOT-23-5; moved to B.Cu
- U11, U15: value UC3525 -> EL817; footprint Package_SO:SOIC-16W_7.5x10.3mm_P1.27mm -> Package_DIP:DIP-4_W7.62mm
- U12, U16: value IRS21867S -> UC3525; footprint Package_SO:SOIC-8_3.9x4.9mm_P1.27mm -> Package_SO:SOIC-16W_7.5x10.3mm_P1.27mm
- U13: value TL432DBZ -> IRS21867S; footprint Package_TO_SOT_SMD:SOT-23-3 -> Package_SO:SOIC-8_3.9x4.9mm_P1.27mm
- U14: value EL817 -> TL432DBZ; footprint Package_DIP:DIP-4_W7.62mm -> Package_TO_SOT_SMD:SOT-23-3
- U17: value EL817 -> OP213ESZ; footprint Package_DIP:DIP-4_W7.62mm -> Package_SO:SO-8_3.9x4.9mm_P1.27mm
- U18: value INA169 -> IRS21867S; footprint Package_TO_SOT_SMD:SOT-23-5 -> Package_SO:SOIC-8_3.9x4.9mm_P1.27mm
- U19: value TL431DBZ -> EL817; footprint Package_TO_SOT_SMD:SOT-23 -> Package_DIP:DIP-4_W7.62mm
- U2: value EL817 -> R7731; footprint Package_DIP:DIP-4_W7.62mm -> Package_TO_SOT_SMD:SOT-23-6; moved to B.Cu
- U20: value ATtiny1616-M -> INA169; footprint Package_DFN_QFN:VQFN-20-1EP_3x3mm_P0.4mm_EP1.7x1.7mm -> Package_TO_SOT_SMD:SOT-23-5
- U21: value ISO1540 -> TL431DBZ; footprint Package_SO:SOIC-8_3.9x4.9mm_P1.27mm -> Package_TO_SOT_SMD:SOT-23
- U4: value L7805ABV -> EL817; footprint Package_TO_SOT_THT:TO-220-3_Vertical -> Package_DIP:DIP-4_W7.62mm
- U6: value TL431DBZ -> L7805ABV; footprint Package_TO_SOT_SMD:SOT-23 -> Package_TO_SOT_THT:TO-220-3_Vertical
- U7: value EL817 -> TL431DBZ; footprint Package_DIP:DIP-4_W7.62mm -> Package_TO_SOT_SMD:SOT-23
- U8: value TL432DBZ -> EL817; footprint Package_TO_SOT_SMD:SOT-23-3 -> Package_DIP:DIP-4_W7.62mm; moved to B.Cu
- U9: value TL331 -> TL432DBZ; footprint Package_TO_SOT_SMD:SOT-23-5 -> Package_TO_SOT_SMD:SOT-23-3; moved to B.Cu
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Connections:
- C1 pad 1: /5V_PWR Sheet/HV_VCC -> /VSYS_PWR_VCC
- C1 pad 2: /5V_PWR Sheet/HV_GND -> /VSYS_PWR_GND
- C10 pad 1: /pwrcontrol Sheet/VSYS_PWR_GND -> /5V_PWR Sheet/HV_VCC
- C10 pad 2: Net-(Q3-D) -> /5V_PWR Sheet/HV_GND
- C11 pad 1: /5V_PWR Sheet/HV_GND -> /VSYS_GND
- C11 pad 2: /5V_PWR Sheet/HV_VCC -> Net-(Q2-D)
- C12 pad 1: Net-(D4-K) -> /VSYS_PWR_GND
- C12 pad 2: /5V_PWR Sheet/STB_GND -> Net-(Q3-D)
- C13 pad 1: /standby Sheet/VSYS1_PRE_VCC -> /5V_PWR Sheet/HV_GND
- C13 pad 2: /VSYS_GND -> /5V_PWR Sheet/HV_VCC
- C14 pad 1: /standby Sheet/VSYS2_PRE_VCC -> Net-(D5-K)
- C14 pad 2: /pwrcontrol Sheet/VSYS_PWR_GND -> /5V_PWR Sheet/STB_GND
- C15 pad 1: Net-(U4-OUT) -> /standby Sheet/VSYS1_PRE_VCC
- C16 pad 1: Net-(U5-OUT) -> /standby Sheet/VSYS2_PRE_VCC
- C16 pad 2: /pwrcontrol Sheet/VSYS_PWR_GND -> /VSYS_PWR_GND
- C17 pad 1: /VSYS_VCC -> Net-(U5-OUT)
- C18 pad 1: /pwrcontrol Sheet/VSYS_PWR -> Net-(U6-OUT)
- C18 pad 2: /pwrcontrol Sheet/VSYS_PWR_GND -> /VSYS_PWR_GND
- C19 pad 1: /5V_PWR Sheet/HV_GND -> Net-(D10-A)
- C19 pad 2: /standby Sheet/FEEDBACK -> /VSYS_GND
- C2 pad 1: /5V_PWR Sheet/HV_GND -> /VSYS_VCC
- C2 pad 2: /5V_PWR Sheet/HV_VCC -> /VSYS_GND
- C20 pad 1: /VSYS_VCC -> Net-(D11-A)
- C20 pad 2: /VSYS_GND -> /VSYS_PWR_GND
- C21 pad 1: /pwrcontrol Sheet/VSYS_PWR -> /5V_PWR Sheet/HV_GND
- C21 pad 2: /pwrcontrol Sheet/VSYS_PWR_GND -> /standby Sheet/FEEDBACK
- C22 pad 1: /standby Sheet/STB_READY_VREF -> Net-(D10-A)
- C22 pad 2: /5V_PWR Sheet/STB_GND -> /VSYS_GND
- C23 pad 1: /5V_PWR Sheet/STB_GND -> Net-(D11-A)
- C23 pad 2: Net-(U8-REF) -> /VSYS_PWR_GND
- C24 pad 1: Net-(D9-A) -> /standby Sheet/STB_READY_VREF
- C25 pad 2: /standby Sheet/IS_VSTANDBY_OK# -> Net-(U9-REF)
- C26 pad 1: Net-(U9--) -> Net-(D12-A)
- C27 pad 1: /5V_PWR Sheet/STB_VCC -> /5V_PWR Sheet/STB_GND
- C27 pad 2: /5V_PWR Sheet/STB_GND -> /standby Sheet/IS_VSTANDBY_OK#
- C28 pad 1: /5V_PWR Sheet/DCDC_5V_VREF -> Net-(U10--)
- C29 pad 1: /5V_PWR Sheet/STB_VCC -> /standby Sheet/STB_VCC
- C3 pad 1: /5V_PWR Sheet/HV_GND -> /standby Sheet/HV_VCC_FUSE
- C3 pad 2: Net-(D2-K) -> /5V_PWR Sheet/HV_GND
- C30 pad 1: Net-(U11-COMP) -> /5V_PWR Sheet/DCDC_5V_VREF
- C31 pad 1: /5V_PWR Sheet/DCDC_FEEDBACK -> /5V_PWR Sheet/DCDC_SHUTDOWN
- C32 pad 1: Net-(U11-CT) -> /5V_PWR Sheet/STB_VCC
- C33 pad 1: /5V_PWR Sheet/STB_GND -> Net-(U12-COMP)
- C33 pad 2: /5V_PWR Sheet/STB_VCC -> /5V_PWR Sheet/STB_GND
- C34 pad 1: Net-(U11-SS) -> /5V_PWR Sheet/DCDC_FEEDBACK
- C35 pad 1: /5V_PWR Sheet/STB_VCC -> Net-(U12-CT)
- C36 pad 1: Net-(D11-K) -> /5V_PWR Sheet/STB_GND
- C36 pad 2: Net-(Q5-S) -> /5V_PWR Sheet/STB_VCC
- C37 pad 1: /5V_PWR Sheet/HV_VCC -> Net-(U12-SS)
- C37 pad 2: /5V_PWR Sheet/HV_GND -> /5V_PWR Sheet/STB_GND
- C38 pad 1: Net-(C38-Pad1) -> /5V_PWR Sheet/STB_VCC
- C38 pad 2: /5V_PWR Sheet/HV_VCC -> /5V_PWR Sheet/STB_GND
- C39 pad 1: /5V_PWR Sheet/HV_GND -> Net-(D15-K)
- C39 pad 2: /5V_PWR Sheet/HV_VCC -> Net-(Q5-S)
- C4 pad 2: Net-(U1-CS) -> /standby Sheet/HV_VCC_FUSE
- C40 pad 1: /5V_PWR Sheet/HV_GND -> /5V_PWR Sheet/HV_VCC_FUSE
- C40 pad 2: Net-(C38-Pad1) -> /5V_PWR Sheet/HV_GND
- C41 pad 1: Net-(D12-K) -> Net-(C41-Pad1)
- C41 pad 2: /+5V_PWR_GND -> /5V_PWR Sheet/HV_VCC_FUSE
- C42 pad 1: /+5V_PWR_GND -> /5V_PWR Sheet/HV_GND
- C42 pad 2: Net-(D12-K) -> /5V_PWR Sheet/HV_VCC_FUSE
- C43 pad 1: /+5V_PWR_VCC -> /5V_PWR Sheet/HV_GND
- C43 pad 2: /+5V_PWR_GND -> Net-(C41-Pad1)
- C44 pad 1: /+5V_PWR_VCC -> Net-(D16-K)
- C45 pad 1: Net-(U13-REF) -> /+5V_PWR_GND
- C45 pad 2: /5V_PWR Sheet/FEEDBACK -> Net-(D16-K)
- C46 pad 1: /+5V_PWR_GND -> /+5V_PWR_VCC
- C46 pad 2: /+5V_PWR_VCC -> /+5V_PWR_GND
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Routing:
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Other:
- board outline added: 120 x 200 mm
